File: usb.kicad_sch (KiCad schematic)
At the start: 11 parts, among them Con5 USB_C_Wurth_632723300011, U8 USBLC6-2, U9 USBLC6-2

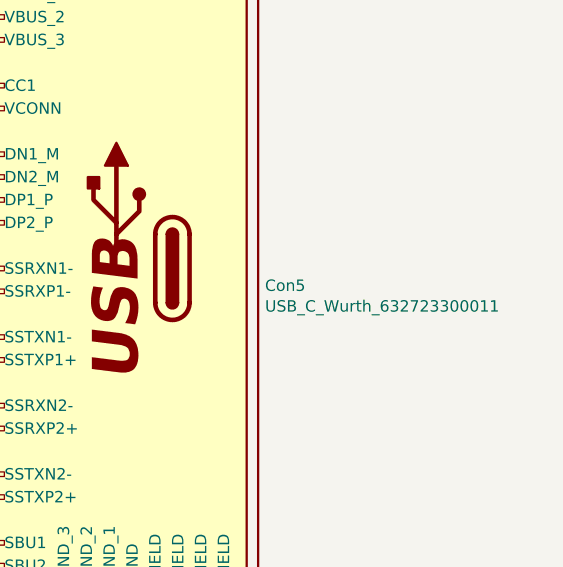
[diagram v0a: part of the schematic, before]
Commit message: Corrected schematic
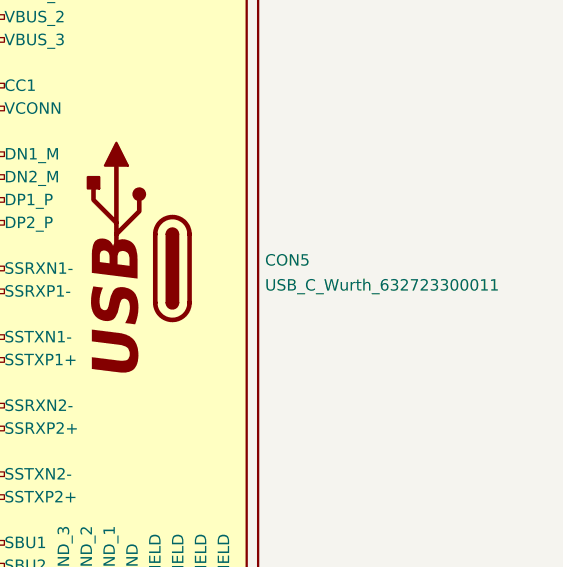
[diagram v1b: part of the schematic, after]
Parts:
- renumbered Con5 to CON5
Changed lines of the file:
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@@
   (symbol (lib_id "USB_Connectors:USB_C_Wurth_632723300011") (at 236.22 119.38 0) (mirror y) (unit 1)
     (in_bom yes) (on_board yes) (fields_autoplaced)
-    (property "Reference" "Con5" (id 0) (at 252.2221 121.2861 0)
+    (property "Reference" "CON5" (id 0) (at 252.222 118.4715 0)
       (effects (font (size 1.27 1.27)) (justify right))
     )
-    (property "Value" "USB_C_Wurth_632723300011" (id 1) (at 252.2221 123.5848 0)
+    (property "Value" "USB_C_Wurth_632723300011" (id 1) (at 252.222 121.2466 0)
       (effects (font (size 1.27 1.27)) (justify right))
     )

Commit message: Tracking in progress
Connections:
- net USB-A-D_N: now also U9.3; no longer U9.1
- net USB-A-D_P: now also U9.1; no longer U9.3
- net at USB1.2 (D-): now also U9.4; no longer U9.6
- net at USB1.3 (D+): now also U9.6; no longer U9.4
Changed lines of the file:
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@@
     (pin "6")
   )
-  (symbol (lib_id "esd_protectors:USBLC6-2") (at 166.37 218.44 270) (unit 1)
+  (symbol (lib_id "esd_protectors:USBLC6-2") (at 166.37 218.44 270) (mirror x) (unit 1)
     (in_bom yes) (on_board yes)
-    (property "Reference" "U9" (id 0) (at 166.37 205.359 90))
-    (property "Value" "USBLC6-2" (id 1) (at 166.37 207.6704 90))
-    (property "Footprint" "ESD_Protectors:USBLC6-2_SOT23-6L" (id 2) (at 166.37 219.71 0)
+    (property "Reference" "U9" (id 0) (at 166.37 208.28 90))
+    (property "Value" "USBLC6-2" (id 1) (at 166.37 229.2096 90))
+    (property "Footprint" "ESD_Protectors:USBLC6-2_SOT23-6L" (id 2) (at 166.37 217.17 0)
       (effects (font (size 1.27 1.27)) hide)
     )
-    (property "Datasheet" "https://www.tme.eu/Document/db59d28d28a96c34f26d05f234ff409c/USBLC6-2.pdf" (id 3) (at 166.37 219.71 0)
+    (property "Datasheet" "https://www.tme.eu/Document/db59d28d28a96c34f26d05f234ff409c/USBLC6-2.pdf" (id 3) (at 166.37 217.17 0)
       (effects (font (size 1.27 1.27)) hide)
     )

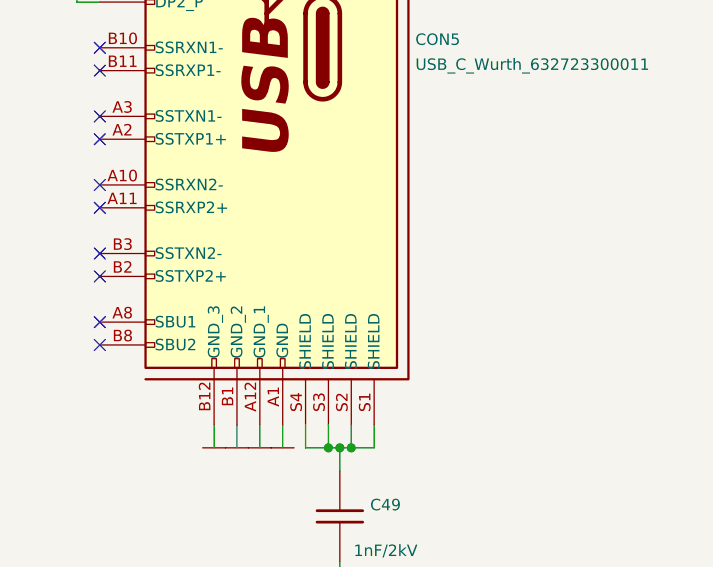
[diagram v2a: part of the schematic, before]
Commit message: Cleared all errors DRC
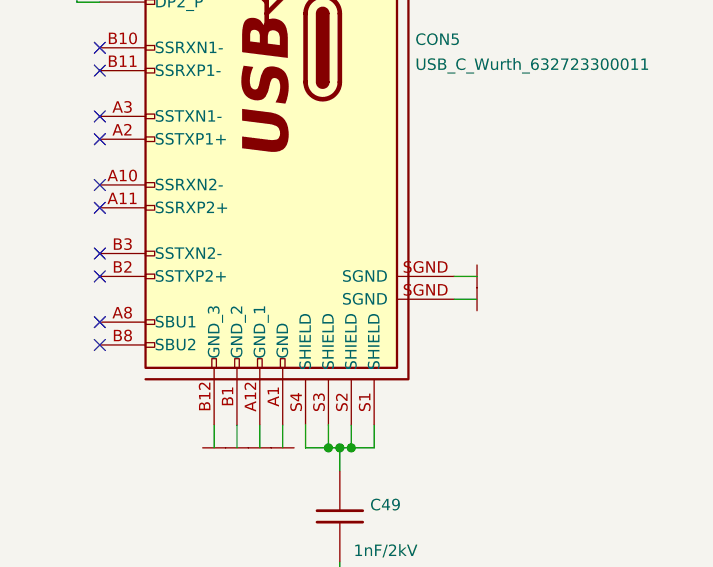
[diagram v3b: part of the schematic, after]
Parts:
- C45, C49: symbol Capacitors_Smd1206:1nF_2kV_1206 -> Capacitors_Smd1206:1nF_2kV; Developer WP -> MW; LCSC Part #(optional) (none) -> C282813; Supplier TME -> Tme
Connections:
- net GND: now also CON5.SGND
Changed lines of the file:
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@@
+    (stroke (width 0) (type solid) (color 0 0 0 0))
+  )
+  (wire (pts (xy 256.54 147.32) (xy 259.08 147.32))
     (stroke (width 0) (type solid) (color 0 0 0 0))
   )
@@
   )
   (wire (pts (xy 205.74 95.25) (xy 166.37 95.25))
+    (stroke (width 0) (type solid) (color 0 0 0 0))
+  )
+  (wire (pts (xy 256.54 144.78) (xy 259.08 144.78))
     (stroke (width 0) (type solid) (color 0 0 0 0))
   )
@@
     (pin "1")
   )
-  (symbol (lib_id "Capacitors_Smd1206:1nF_2kV_1206") (at 243.84 171.45 180) (unit 1)
+  (symbol (lib_id "Capacitors_Smd1206:1nF_2kV") (at 243.84 171.45 180) (unit 1)
     (in_bom yes) (on_board yes)
     (property "Reference" "C49" (id 0) (at 248.92 170.18 0))
@@
       (effects (font (size 1.27 1.27)) hide)
     )
-    (property "Datasheet" "Capacitors/Smd_1206/Components_Documentation/1nF_2kV_1206.pdf" (id 3) (at 248.92 173.99 0)
+    (property "Datasheet" "https://www.tme.eu/Document/fbb9415081fcefba62c0f8bbf5b21210/UPY-GPHC_X7R_6.3V-to-50V_20.pdf" (id 3) (at 248.92 173.99 0)
       (effects (font (size 1.27 1.27)) hide)
     )
@@
       (effects (font (size 1.27 1.27)) hide)
     )
-    (property "Supplier" "TME" (id 6) (at 243.84 171.45 0)
+    (property "Supplier" "Tme" (id 6) (at 243.84 171.45 0)
       (effects (font (size 1.27 1.27)) hide)
     )
@@
       (effects (font (size 1.27 1.27)) hide)
     )
-    (property "Developer" "WP" (id 11) (at 243.84 171.45 0)
+    (property "Developer" "MW" (id 11) (at 243.84 171.45 0)
       (effects (font (size 1.27 1.27)) hide)
     )
@@
       (effects (font (size 1.27 1.27)) hide)
     )
+    (property "LCSC Part #(optional)" "C282813" (id 13) (at 243.84 171.45 0)
+      (effects (font (size 1.27 1.27)) hide)
+    )
     (pin "1")
     (pin "2")
@@
     (pin "1")
   )
-  (symbol (lib_id "Capacitors_Smd1206:1nF_2kV_1206") (at 220.98 232.41 180) (unit 1)
+  (symbol (lib_id "Capacitors_Smd1206:1nF_2kV") (at 220.98 232.41 180) (unit 1)
     (in_bom yes) (on_board yes)
     (property "Reference" "C45" (id 0) (at 226.06 231.14 0))
@@
       (effects (font (size 1.27 1.27)) hide)
     )
-    (property "Datasheet" "Capacitors/Smd_1206/Components_Documentation/1nF_2kV_1206.pdf" (id 3) (at 226.06 234.95 0)
+    (property "Datasheet" "https://www.tme.eu/Document/fbb9415081fcefba62c0f8bbf5b21210/UPY-GPHC_X7R_6.3V-to-50V_20.pdf" (id 3) (at 226.06 234.95 0)
       (effects (font (size 1.27 1.27)) hide)
     )
@@
       (effects (font (size 1.27 1.27)) hide)
     )
-    (property "Supplier" "TME" (id 6) (at 220.98 232.41 0)
+    (property "Supplier" "Tme" (id 6) (at 220.98 232.41 0)
       (effects (font (size 1.27 1.27)) hide)
     )
@@
       (effects (font (size 1.27 1.27)) hide)
     )
-    (property "Developer" "WP" (id 11) (at 220.98 232.41 0)
+    (property "Developer" "MW" (id 11) (at 220.98 232.41 0)
       (effects (font (size 1.27 1.27)) hide)
     )
@@
       (effects (font (size 1.27 1.27)) hide)
     )
+    (property "LCSC Part #(optional)" "C282813" (id 13) (at 220.98 232.41 0)
+      (effects (font (size 1.27 1.27)) hide)
+    )
     (pin "1")
     (pin "2")
+  )
+  (symbol (lib_id "power:GND") (at 259.08 144.78 90) (unit 1)
+    (in_bom yes) (on_board yes)
+    (property "Reference" "#PWR0226" (id 0) (at 256.54 144.78 0)
+      (effects (font (size 0.762 0.762)) hide)
+    )
+    (property "Value" "GND" (id 1) (at 261.62 144.78 0)
+      (effects (font (size 0.762 0.762)) hide)
+    )
+    (property "Footprint" "" (id 2) (at 259.08 144.78 0)
+      (effects (font (size 1.524 1.524)))
+    )
+    (property "Datasheet" "" (id 3) (at 259.08 144.78 0)
+      (effects (font (size 1.524 1.524)))
+    )
+    (pin "1")
+  )
+  (symbol (lib_id "power:GND") (at 259.08 147.32 90) (unit 1)
+    (in_bom yes) (on_board yes)
+    (property "Reference" "#PWR0227" (id 0) (at 256.54 147.32 0)
+      (effects (font (size 0.762 0.762)) hide)
+    )
+    (property "Value" "GND" (id 1) (at 261.62 147.32 0)
+      (effects (font (size 0.762 0.762)) hide)
+    )
+    (property "Footprint" "" (id 2) (at 259.08 147.32 0)
+      (effects (font (size 1.524 1.524)))
+    )
+    (property "Datasheet" "" (id 3) (at 259.08 147.32 0)
+      (effects (font (size 1.524 1.524)))
+    )
+    (pin "1")
   )
   (symbol (lib_id "USB_Connectors:USB_C_Wurth_632723300011") (at 236.22 119.38 0) (mirror y) (unit 1)
@@
       (effects (font (size 1.27 1.27)) hide)
     )
+    (property "LCSC Part #(optional)" "" (id 13) (at 236.22 119.38 0))
     (pin "A1")
     (pin "A10")
@@
     (pin "S3")
     (pin "S4")
+    (pin "SGND")
+    (pin "SGND")
   )
 )

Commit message: Eliminated all warnings realted with footprints
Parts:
- C46, C48: footprint Capacitors_Smd_0603:100nF_0603 -> Capacitors_Smd_0402:100nF_0402; symbol Capacitors_Smd0603:100n -> Capacitors_Smd0402:100nF; Developer (none) -> MW; LCSC Part # (optional) (none) -> C131394; Manufacturer SAMSUNG -> Murata; Manufacturer Part Number CL10B104JB8NNNC -> GRM155R71H104KE14D; Package 0603 -> 0402; Package_1 (none) -> 0402; Price@1000pcs 0,02231 -> 0,03299; Price@1pc 0,04540 -> 0,07091; Supplier TME -> Tme; Supplier Part Number CL10B104JB8NNNC -> GRM155R71H104KE14D; URL https://www.tme.eu/pl/details/cl10b104jb8nnnc/kondensatory-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 -> https://www.tme.eu/pl/details/grm155r71h104ke14d/kondensato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
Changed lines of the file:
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@@
     (pin "2")
   )
-  (symbol (lib_id "Capacitors_Smd0603:100n") (at 242.57 196.85 0) (unit 1)
+  (symbol (lib_id "Capacitors_Smd0402:100nF") (at 242.57 196.85 0) (unit 1)
     (in_bom yes) (on_board yes)
     (property "Reference" "C46" (id 0) (at 245.8974 195.6816 0)
@@
       (effects (font (size 1.27 1.27)) (justify left))
     )
-    (property "Footprint" "Capacitors_Smd_0603:100nF_0603" (id 2) (at 242.57 196.85 0)
-      (effects (font (size 1.524 1.524)) hide)
-    )
-    (property "Datasheet" "Capacitors/Smd_0603/Components_Documentation/KEM_C1005_Y5V_SMD.pdf" (id 3) (at 242.57 196.85 0)
-      (effects (font (size 1.524 1.524)) hide)
-    )
-    (property "Manufacturer" "SAMSUNG" (id 4) (at 242.57 196.85 0)
-      (effects (font (size 1.27 1.27)) hide)
-    )
-    (property "Manufacturer Part Number" "CL10B104JB8NNNC" (id 5) (at 242.57 196.85 0)
-      (effects (font (size 1.27 1.27)) hide)
-    )
-    (property "Supplier" "TME" (id 6) (at 242.57 196.85 0)
-      (effects (font (size 1.27 1.27)) hide)
-    )
-    (property "Supplier Part Number" "CL10B104JB8NNNC" (id 7) (at 242.57 196.85 0)
-      (effects (font (size 1.27 1.27)) hide)
-    )
-    (property "URL" "https://www.tme.eu/pl/details/cl10b104jb8nnnc/kondensatory-mlcc-smd-0603/samsung/" (id 8) (at 242.57 196.85 0)
-      (effects (font (size 1.27 1.27)) hide)
-    )
-    (property "Price@1pc" "0,04540" (id 9) (at 242.57 196.85 0)
-      (effects (font (size 1.27 1.27)) hide)
-    )
-    (property "Price@1000pcs" "0,02231" (id 10) (at 242.57 196.85 0)
-      (effects (font (size 1.27 1.27)) hide)
-    )
-    (property "Package" "0603" (id 11) (at 242.57 196.85 0)
+    (property "Footprint" "Capacitors_Smd_0402:100nF_0402" (id 2) (at 242.57 196.85 0)
+      (effects (font (size 1.27 1.27)) hide)
+    )
+    (property "Datasheet" "https://www.tme.eu/Document/558f361ed82994aff5a3e7789d970dd1/GRM155R71H104KE14-01.pdf" (id 3) (at 242.57 196.85 0)
+      (effects (font (size 1.27 1.27)) hide)
+    )
+    (property "Manufacturer" "Murata" (id 4) (at 242.57 196.85 0)
+      (effects (font (size 1.27 1.27)) hide)
+    )
+    (property "Manufacturer Part Number" "GRM155R71H104KE14D" (id 5) (at 242.57 196.85 0)
+      (effects (font (size 1.27 1.27)) hide)
+    )
+    (property "Supplier" "Tme" (id 6) (at 242.57 196.85 0)
+      (effects (font (size 1.27 1.27)) hide)
+    )
+    (property "Supplier Part Number" "GRM155R71H104KE14D" (id 7) (at 242.57 196.85 0)
+      (effects (font (size 1.27 1.27)) hide)
+    )
+    (property "URL" "https://www.tme.eu/pl/details/grm155r71h104ke14d/kondensatory-mlcc-smd-0402/murata/" (id 8) (at 242.57 196.85 0)
+      (effects (font (size 1.27 1.27)) hide)
+    )
+    (property "Price@1pc" "0,07091" (id 9) (at 242.57 196.85 0)
+      (effects (font (size 1.27 1.27)) hide)
+    )
+    (property "Price@1000pcs" "0,03299" (id 10) (at 242.57 196.85 0)
+      (effects (font (size 1.27 1.27)) hide)
+    )
+    (property "Package" "0402" (id 11) (at 242.57 196.85 0)
+      (effects (font (size 1.27 1.27)) hide)
+    )
+    (property "Developer" "MW" (id 12) (at 242.57 196.85 0)
+      (effects (font (size 1.27 1.27)) hide)
+    )
+    (property "Package_1" "0402" (id 13) (at 242.57 196.85 0)
+      (effects (font (size 1.27 1.27)) hide)
+    )
+    (property "LCSC Part # (optional)" "C131394" (id 14) (at 242.57 196.85 0)
       (effects (font (size 1.27 1.27)) hide)
     )
@@
     (pin "2")
   )
-  (symbol (lib_id "Capacitors_Smd0603:100n") (at 241.3 71.12 0) (unit 1)
+  (symbol (lib_id "Capacitors_Smd0402:100nF") (at 241.3 71.12 0) (unit 1)
     (in_bom yes) (on_board yes)
     (property "Reference" "C48" (id 0) (at 244.6274 69.9516 0)
@@
       (effects (font (size 1.27 1.27)) (justify left))
     )
-    (property "Footprint" "Capacitors_Smd_0603:100nF_0603" (id 2) (at 241.3 71.12 0)
-      (effects (font (size 1.524 1.524)) hide)
-    )
-    (property "Datasheet" "Capacitors/Smd_0603/Components_Documentation/KEM_C1005_Y5V_SMD.pdf" (id 3) (at 241.3 71.12 0)
-      (effects (font (size 1.524 1.524)) hide)
-    )
-    (property "Manufacturer" "SAMSUNG" (id 4) (at 241.3 71.12 0)
-      (effects (font (size 1.27 1.27)) hide)
-    )
-    (property "Manufacturer Part Number" "CL10B104JB8NNNC" (id 5) (at 241.3 71.12 0)
-      (effects (font (size 1.27 1.27)) hide)
-    )
-    (property "Supplier" "TME" (id 6) (at 241.3 71.12 0)
-      (effects (font (size 1.27 1.27)) hide)
-    )
-    (property "Supplier Part Number" "CL10B104JB8NNNC" (id 7) (at 241.3 71.12 0)
-      (effects (font (size 1.27 1.27)) hide)
-    )
-    (property "URL" "https://www.tme.eu/pl/details/cl10b104jb8nnnc/kondensatory-mlcc-smd-0603/samsung/" (id 8) (at 241.3 71.12 0)
-      (effects (font (size 1.27 1.27)) hide)
-    )
-    (property "Price@1pc" "0,04540" (id 9) (at 241.3 71.12 0)
-      (effects (font (size 1.27 1.27)) hide)
-    )
-    (property "Price@1000pcs" "0,02231" (id 10) (at 241.3 71.12 0)
-      (effects (font (size 1.27 1.27)) hide)
-    )
-    (property "Package" "0603" (id 11) (at 241.3 71.12 0)
-      (effects (font (size 1.27 1.27)) hide)
-    )
+    (property "Footprint" "Capacitors_Smd_0402:100nF_0402" (id 2) (at 241.3 71.12 0)
+      (effects (font (size 1.27 1.27)) hide)
+    )
+    (property "Datasheet" "https://www.tme.eu/Document/558f361ed82994aff5a3e7789d970dd1/GRM155R71H104KE14-01.pdf" (id 3) (at 241.3 71.12 0)
+      (effects (font (size 1.27 1.27)) hide)
+    )
+    (property "Manufacturer" "Murata" (id 4) (at 241.3 71.12 0)
+      (effects (font (size 1.27 1.27)) hide)
+    )
+    (property "Manufacturer Part Number" "GRM155R71H104KE14D" (id 5) (at 241.3 71.12 0)
+      (effects (font (size 1.27 1.27)) hide)
+    )
+    (property "Supplier" "Tme" (id 6) (at 241.3 71.12 0)
+      (effects (font (size 1.27 1.27)) hide)
+    )
+    (property "Supplier Part Number" "GRM155R71H104KE14D" (id 7) (at 241.3 71.12 0)
+      (effects (font (size 1.27 1.27)) hide)
+    )
+    (property "URL" "https://www.tme.eu/pl/details/grm155r71h104ke14d/kondensatory-mlcc-smd-0402/murata/" (id 8) (at 241.3 71.12 0)
+      (effects (font (size 1.27 1.27)) hide)
+    )
+    (property "Price@1pc" "0,07091" (id 9) (at 241.3 71.12 0)
+      (effects (font (size 1.27 1.27)) hide)
+    )
+    (property "Price@1000pcs" "0,03299" (id 10) (at 241.3 71.12 0)
+      (effects (font (size 1.27 1.27)) hide)
+    )
+    (property "Package" "0402" (id 11) (at 241.3 71.12 0)
+      (effects (font (size 1.27 1.27)) hide)
+    )
+    (property "Developer" "MW" (id 12) (at 241.3 71.12 0)
+      (effects (font (size 1.27 1.27)) hide)
+    )
+    (property "Package_1" "0402" (id 13) (at 241.3 71.12 0)
+      (effects (font (size 1.27 1.27)) hide)
+    )
+    (property "LCSC Part # (optional)" "C131394" (id 14) (at 241.3 71.12 0)
+      (effects (font (size 1.27 1.27)) hide)
+    )

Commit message: Gerbers created, BOM, CPL
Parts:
- C46, C48: value 100n -> 100nF/50V
- U8, U9: Manufacturer (none) -> STMicroelectronics; Manufaturer STMicroelectronics -> (none)
